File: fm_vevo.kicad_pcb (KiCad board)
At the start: 2 copper layers, 87.5 x 47.5 mm, 89 parts, among them J1 Hangoló fesz., J2 bemenet2, J3 Bemenet, J4 HO/1024, J5 12VDC, J6 RedPitaya_+-1V, J7 AudioJack, Q1 mmbfj310, Q2 MMBT3904, U1 LM358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

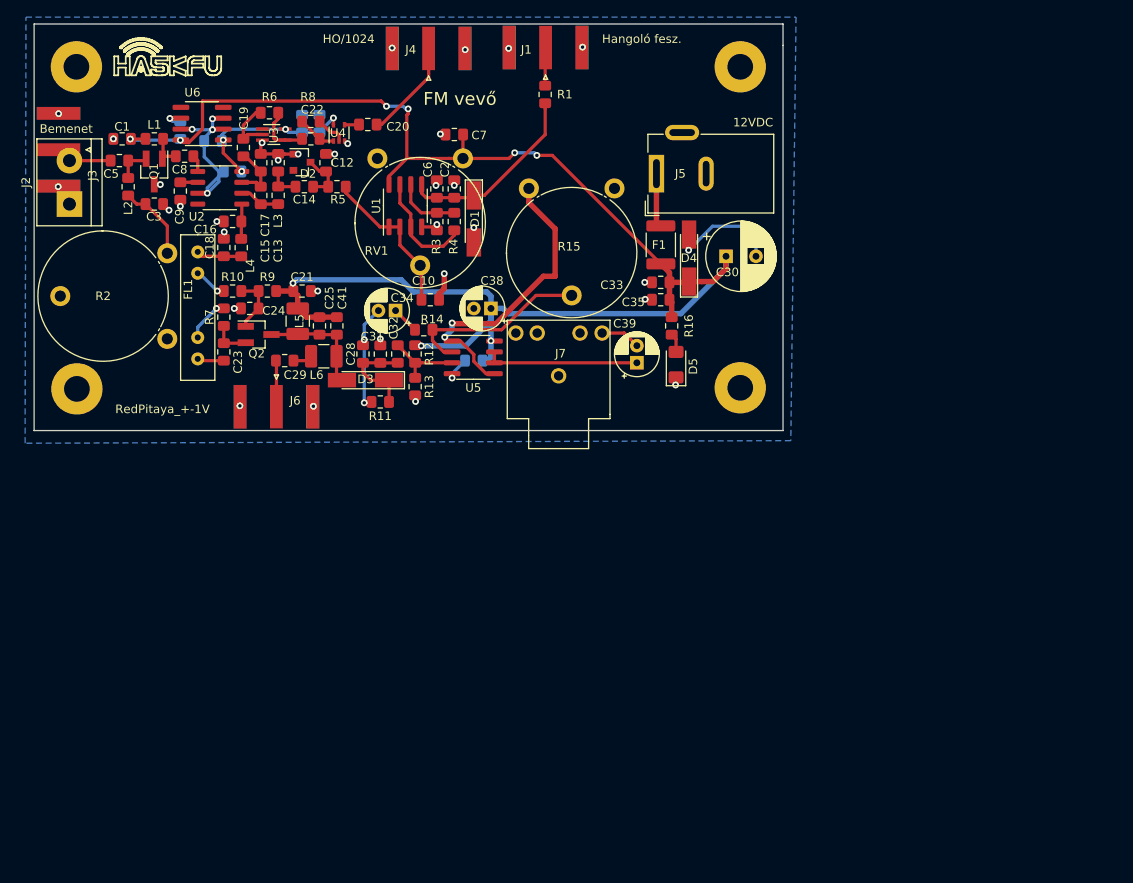
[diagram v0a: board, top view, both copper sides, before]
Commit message: alternate layout
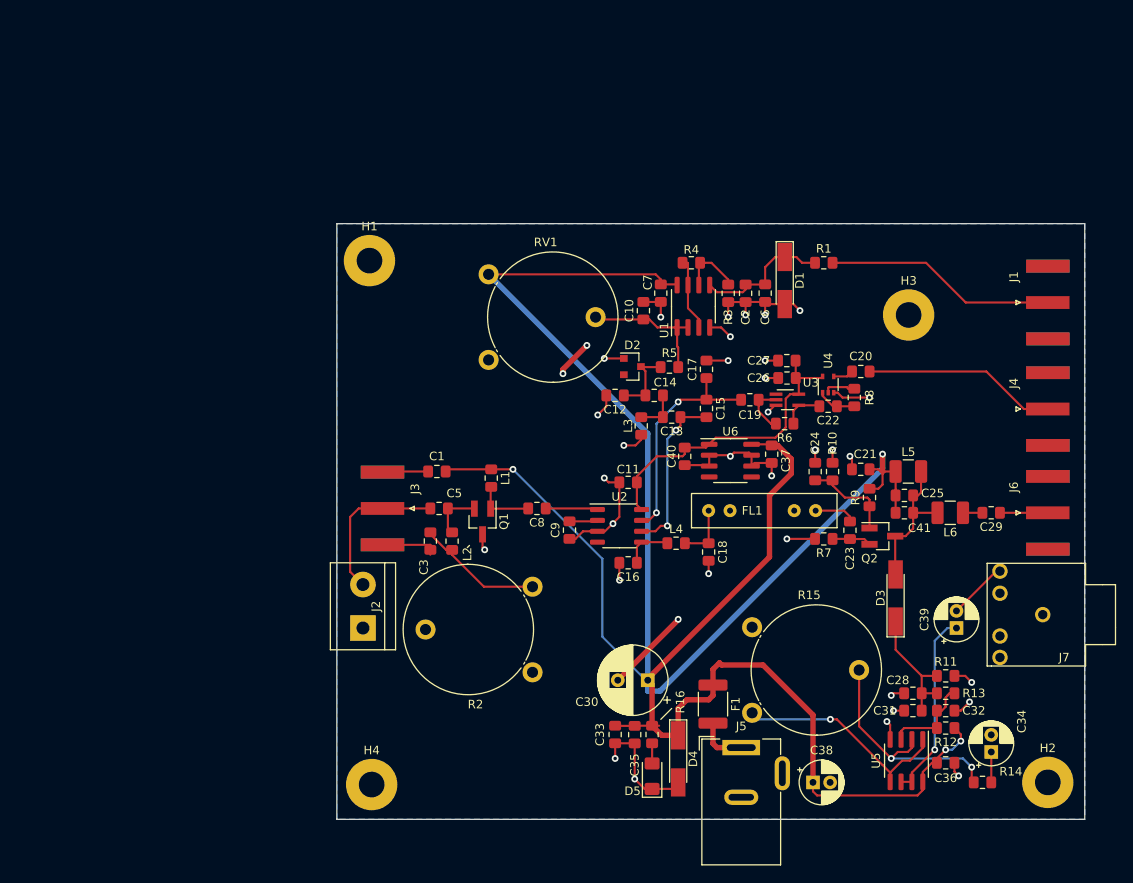
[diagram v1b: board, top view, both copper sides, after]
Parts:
- C11, C26, C27, C36, C37, C40: moved to F.Cu
- J1: value Hangoló fesz. -> RedPitaya_kimenete
- J4: value HO/1024 -> RedPitaya_+-10V
- moved H2 91.0 mm to (138.4, 133.6)
- moved J6 91.0 mm to (138.4, 102.1), turned to 0 degrees
- moved C34 86.6 mm to (131.8, 130.0), turned to 90 degrees
- moved C29 84.4 mm to (131.8, 102.1), turned to 180 degrees
- moved R14 84.0 mm to (130.8, 133.6), turned to 0 degrees
- moved J4 83.7 mm to (138.4, 90.0), turned to 0 degrees
- moved C37 78.8 mm to (106.2, 95.3), turned to 270 degrees
- moved Q2 76.6 mm to (119.1, 104.8)
- moved C23 76.1 mm to (115.3, 104.1), turned to 90 degrees
- moved R12 75.8 mm to (126.5, 127.3), turned to 180 degrees
- moved C28 75.5 mm to (122.7, 123.2), turned to 180 degrees
- moved L6 75.4 mm to (127.0, 102.1), turned to 180 degrees
- moved C32 75.3 mm to (126.5, 123.2), turned to 180 degrees
- moved C31 74.9 mm to (122.7, 125.2), turned to 180 degrees
- moved R7 74.7 mm to (112.3, 105.2), turned to 180 degrees
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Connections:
- U2 pad 4: Net-(U2-Pad4) -> (no net)
- U6 pad 4: Net-(U6-Pad4) -> (no net)
- U6 pad 5: Net-(U6-Pad5) -> (no net)
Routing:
- net +12V: track 187.4 -> 283.2 mm, vias 9 -> 4
- net GND: track 90.7 -> 132.5 mm, vias 43 -> 36
- net Net-(J1-Pad1): track 4.47 -> 27.6 mm
- net Net-(C15-Pad1): track 6.97 -> 26.1 mm, vias 0 -> 2
- net +5V: track 20.3 -> 36.7 mm, vias 4 -> 0
- net Net-(C13-Pad1): track 4.79 -> 19.7 mm, vias 0 -> 2
- net Net-(C5-Pad2): track 6.60 -> 18.3 mm
- net Net-(C20-Pad1): track 11.7 -> 22.6 mm
- net Net-(R15-Pad1): track 36.0 -> 26.1 mm, vias 2 -> 1
- net Net-(C2-Pad1): track 22.4 -> 16.1 mm
- net Net-(C3-Pad1): track 9.25 -> 15.0 mm
- net Net-(R14-Pad1): track 22.0 -> 27.5 mm, vias 0 -> 2
- net Net-(R4-Pad2): track 13.2 -> 8.68 mm
- net Net-(C24-Pad1): track 6.77 -> 10.9 mm
- net Net-(C8-Pad1): track 1.99 -> 6.10 mm
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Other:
- board size 87.5 x 47.5 mm -> 87.4 x 69.6 mm
- board text removed: "2020 tavasz"
- board text removed: "A koronavírus járvány alatt tartott távfoglalkozások eredménye"
- board text removed: "FM vevő"
